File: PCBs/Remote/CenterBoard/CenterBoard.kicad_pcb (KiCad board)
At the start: 4 copper layers, 100 x 100 mm, 92 parts, among them J201 DX07S016JA1R1500, J401 SMA, J501 Conn_01x11, J701 Conn_02x10_Odd_Even, U201 LPC51U68JBD64, U202 W25Q128JVS, U301 SC189ZSKTRT, U401 nRF24L01P, U402 RFX2401C, U501 LP5024, U502 TLC555CDR, U601 Joystick Left, U602 Joystick Right, U701 74HC14, U702 74HC14, U703 74HC14, X401 16MHz

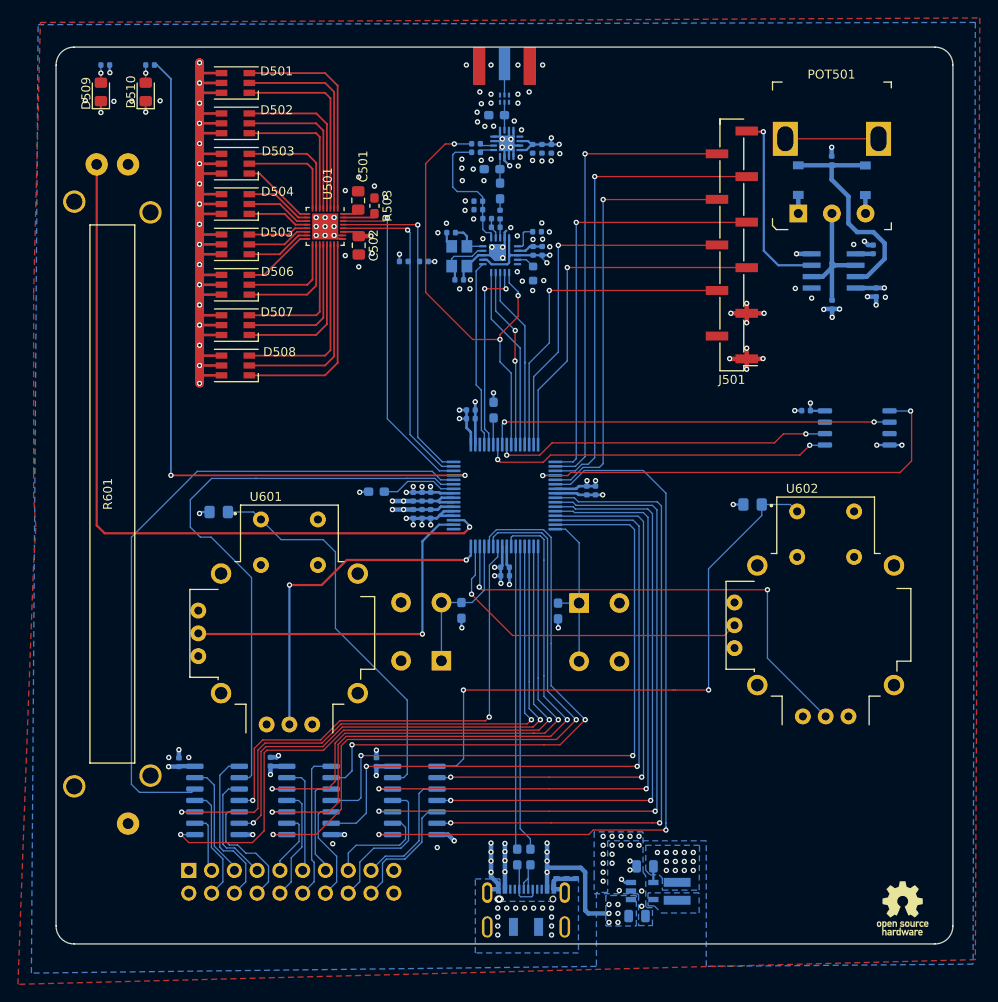
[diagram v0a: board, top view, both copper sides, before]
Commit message: Some cleanup, and PCB antenna removal.
Last edits before asking for reddit feedback.

Signed-off-by: Eldalote.Electronics <Eldalote.Electronics@gmail.com>
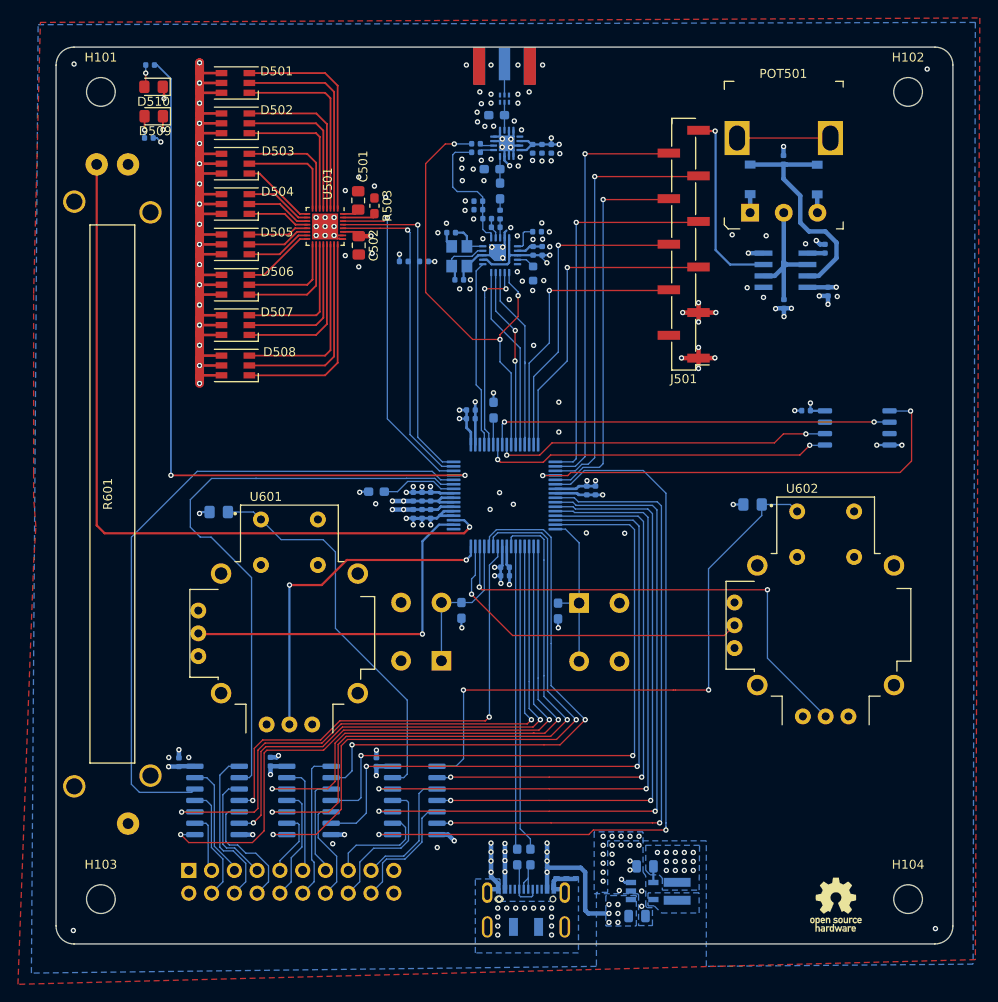
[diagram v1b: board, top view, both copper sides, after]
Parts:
- added H101: MountingHole, MountingHole:MountingHole_3.2mm_M3_ISO7380, F.Cu at (105.0, 65.0)
- added H102: MountingHole, MountingHole:MountingHole_3.2mm_M3_ISO7380, F.Cu at (195.0, 65.0)
- added H103: MountingHole, MountingHole:MountingHole_3.2mm_M3_ISO7380, F.Cu at (105.0, 155.0)
- added H104: MountingHole, MountingHole:MountingHole_3.2mm_M3_ISO7380, F.Cu at (195.0, 155.0)
- moved R501 9.47 mm to (110.3, 70.1)
- moved LOGO101 7.45 mm to (186.9, 155.6)
- moved D509 6.48 mm to (110.9, 67.7), turned to 180 degrees
- moved C503 5.37 mm to (181.2, 88.6)
- moved C504 5.37 mm to (185.7, 82.5)
- moved C505 5.37 mm to (186.1, 87.3)
- moved D511 5.37 mm to (184.9, 74.8)
- moved D512 5.37 mm to (177.4, 74.8)
- moved J501 5.37 mm to (170.0, 82.0)
- moved POT501 5.37 mm to (177.4, 78.5)
- moved R504 5.37 mm to (181.1, 72.6)
- moved U502 5.37 mm to (181.3, 84.9)
- moved D510 1.04 mm to (110.9, 64.4), turned to 180 degrees
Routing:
- net Screen_SPI_MISO: track 41.1 -> 35.8 mm
- net Screen_SPI_SCLK: track 37.0 -> 31.7 mm
- net Screen_TFT_DC: track 53.3 -> 48.0 mm
- net Screen_SPI_CSn_SDCard: track 52.2 -> 47.0 mm
- net Screen_TFT_RESET: track 48.2 -> 43.0 mm
- net Screen_SPI_CSn_TFT: track 47.8 -> 42.6 mm
- net Screen_SPI_MOSI: track 41.1 -> 35.9 mm
- net Net-(D509-Pad2): track 1.84 -> 2.42 mm
- net GND: track 106.0 -> 106.2 mm, vias 160 -> 171
- net (no net): vias 0 -> 1
